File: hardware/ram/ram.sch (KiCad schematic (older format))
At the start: 16 parts, among them J1 I/O Expansion 1, J2 I/O Expansion 2, J3 DB25_Male, J4 DB37_Male, U1 71V016SA12PHGI, U2 SN74HCS00PWR, U3 SN74HCS00PWR, U4 SN74HCS00PWR, U5 SN74LVC541APWR, U6 SN74LVC541APWR

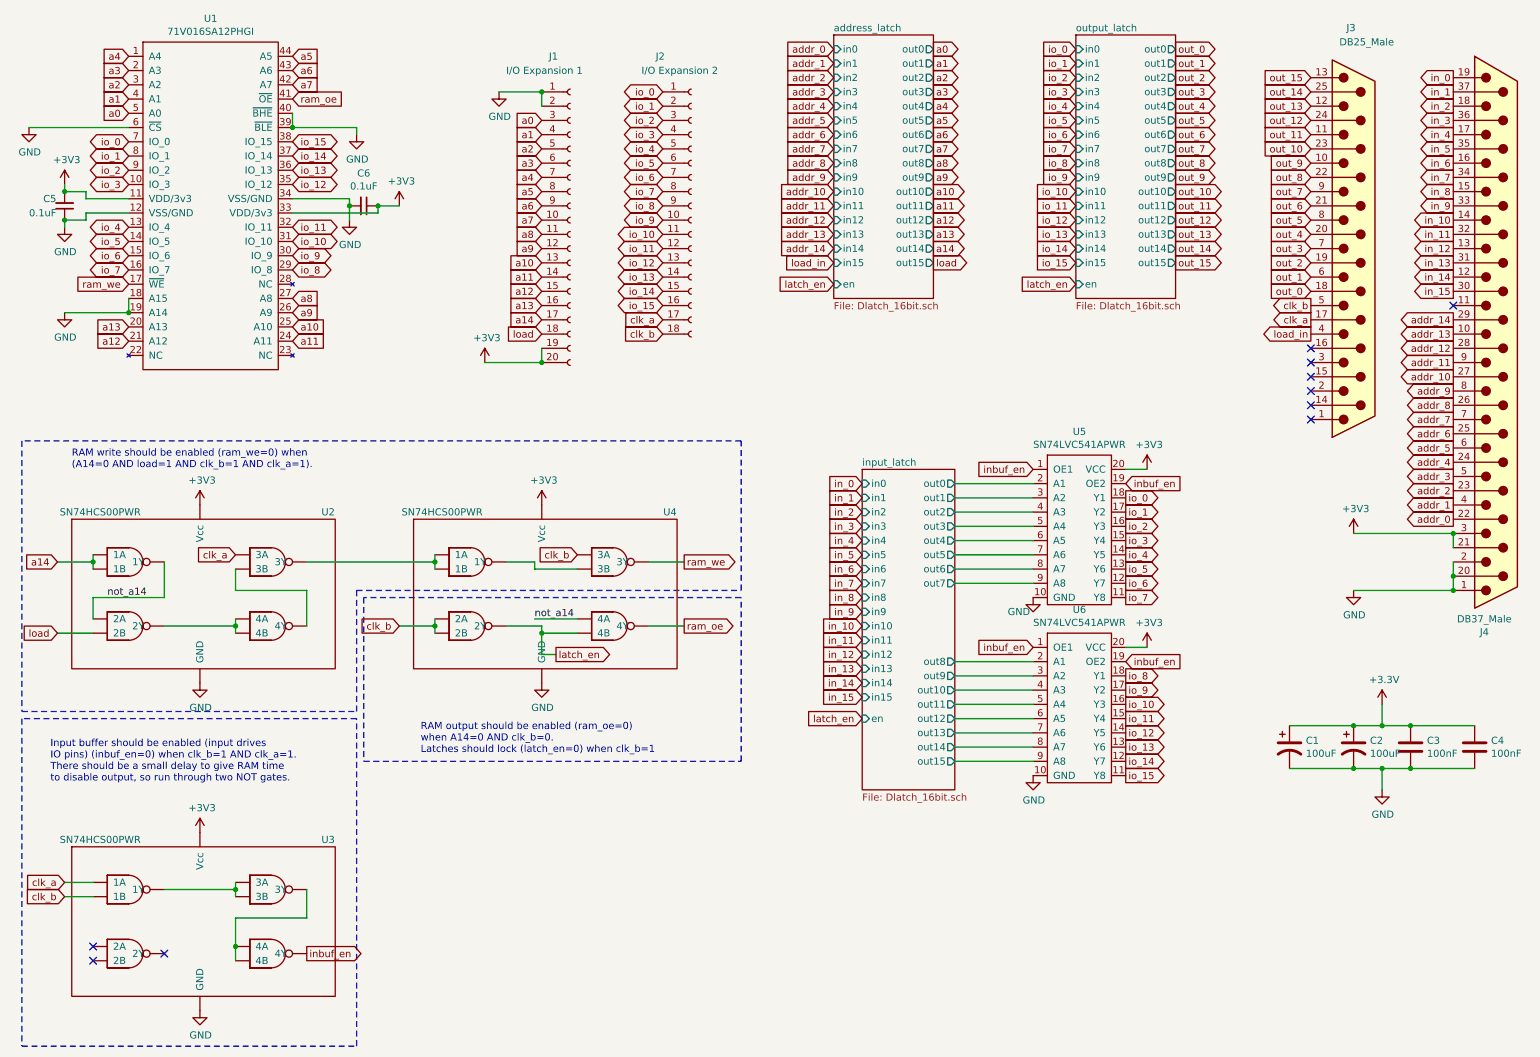
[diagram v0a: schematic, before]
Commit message: RAM board rework complete. Added COTS latch chips and Teensy 4.1 peripheral + magjack for ethernet.
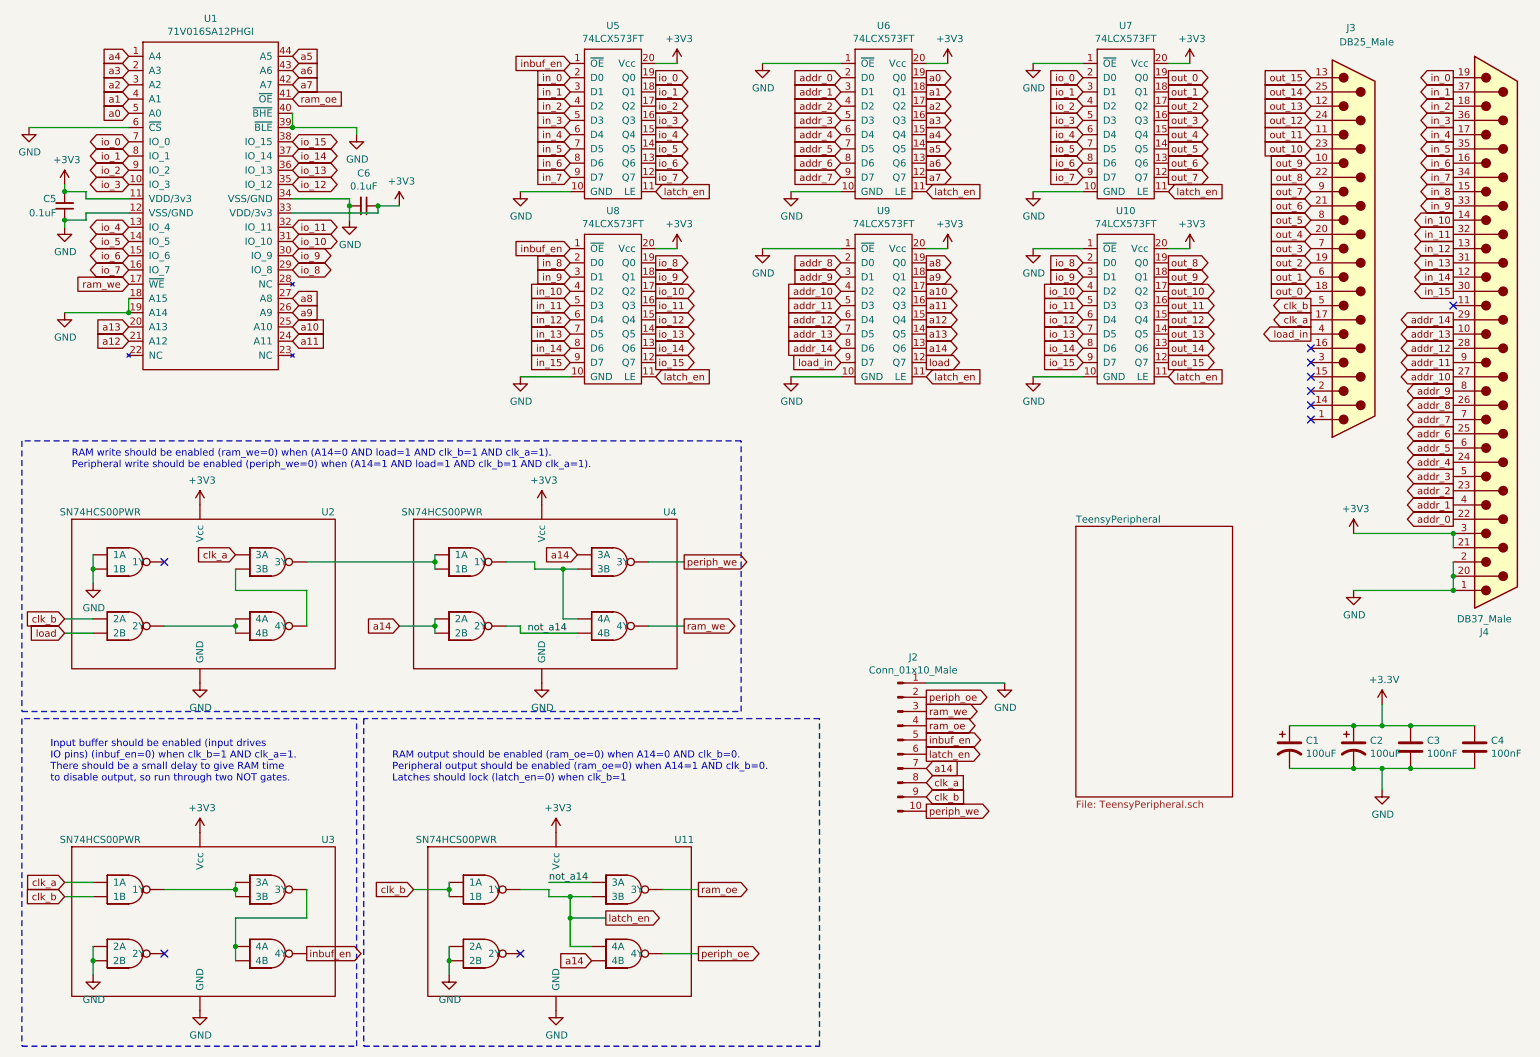
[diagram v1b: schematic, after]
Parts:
- removed J1: I/O Expansion 1, Connector_PinHeader_2.54mm:PinHeader_2x10_P2.54mm_Vertical, symbol Connector:Conn_01x20_Female
- removed J2: I/O Expansion 2, Connector_PinHeader_2.54mm:PinHeader_2x09_P2.54mm_Vertical, symbol Connector:Conn_01x18_Female
- removed U5, U6: SN74LVC541APWR, Package_SO:TSSOP-20_4.4x6.5mm_P0.65mm, symbol NANDIRL_components:SN74LVC541APWR
- added J2: Conn_01x10_Male, Connector_PinHeader_2.54mm:PinHeader_1x10_P2.54mm_Vertical, symbol Connector:Conn_01x10_Male
- added U10, U5, U6, U7, U8, U9: 74LCX573FT, Package_SO:TSSOP-20_4.4x6.5mm_P0.65mm, symbol NANDIRL_components:74LCX573FT
- added U11: SN74HCS00PWR, Package_SO:TSSOP-14_4.4x5mm_P0.65mm, symbol NANDIRL_components:SN74HCS00PWR
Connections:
- net +3V3: now also U10.20 (Vcc), U11.14 (Vcc), U5.20 (Vcc), U6.20 (Vcc), U7.20 (Vcc), U8.20 (Vcc), U9.20 (Vcc)
- net GND: now also U2.1 (1A), U2.2 (1B), U3.4 (2A), U3.5 (2B), J2.1 (Pin_1), U10.1 (~OE), U10.10 (GND), U11.4 (2A), U11.5 (2B), U11.7 (GND), U5.10 (GND), U6.1 (~OE), U6.10 (GND), U7.1 (~OE), U7.10 (GND), U8.10 (GND), U9.1 (~OE), U9.10 (GND)
- net a0: now also U6.19 (Q0)
- net a1: now also U6.18 (Q1)
- net a10: now also U9.17 (Q2)
- net a11: now also U9.16 (Q3)
- net a12: now also U9.15 (Q4)
- net a13: now also U9.14 (Q5)
- net a14: now also U4.4 (2A), U4.5 (2B), U4.9 (3A), J2.7 (Pin_7), U11.13 (4B), U9.13 (Q6); no longer U2.1 (1A), U2.2 (1B)
- net a2: now also U6.17 (Q2)
- net a3: now also U6.16 (Q3)
- net a4: now also U6.15 (Q4)
- net a5: now also U6.14 (Q5)
- net a6: now also U6.13 (Q6)
- net a7: now also U6.12 (Q7)
- net a8: now also U9.19 (Q0)
- net a9: now also U9.18 (Q1)
- net addr_0: now also U6.2 (D0)
- net addr_1: now also U6.3 (D1)
- net addr_10: now also U9.4 (D2)
- net addr_11: now also U9.5 (D3)
- net addr_12: now also U9.6 (D4)
- net addr_13: now also U9.7 (D5)
- net addr_14: now also U9.8 (D6)
- net addr_2: now also U6.4 (D2)
- net addr_3: now also U6.5 (D3)
- net addr_4: now also U6.6 (D4)
- net addr_5: now also U6.7 (D5)
- net addr_6: now also U6.8 (D6)
- net addr_7: now also U6.9 (D7)
- net addr_8: now also U9.2 (D0)
- net addr_9: now also U9.3 (D1)
- net clk_a: now also J2.8 (Pin_8)
- net clk_b: now also U2.4 (2A), J2.9 (Pin_9), U11.1 (1A), U11.2 (1B); no longer U4.4 (2A), U4.5 (2B), U4.9 (3A)
- net in_0: now also U5.2 (D0)
- net in_1: now also U5.3 (D1)
- net in_10: now also U8.4 (D2)
- net in_11: now also U8.5 (D3)
- net in_12: now also U8.6 (D4)
- net in_13: now also U8.7 (D5)
- net in_14: now also U8.8 (D6)
- net in_15: now also U8.9 (D7)
- net in_2: now also U5.4 (D2)
- net in_3: now also U5.5 (D3)
- net in_4: now also U5.6 (D4)
- net in_5: now also U5.7 (D5)
- net in_6: now also U5.8 (D6)
- net in_7: now also U5.9 (D7)
- net in_8: now also U8.2 (D0)
- net in_9: now also U8.3 (D1)
- net inbuf_en: now also J2.5 (Pin_5), U5.1 (~OE), U8.1 (~OE)
- net io_0: now also U5.19 (Q0), U7.2 (D0)
- net io_1: now also U5.18 (Q1), U7.3 (D1)
- net io_10: now also U10.4 (D2), U8.17 (Q2)
- net io_11: now also U10.5 (D3), U8.16 (Q3)
- net io_12: now also U10.6 (D4), U8.15 (Q4)
- net io_13: now also U10.7 (D5), U8.14 (Q5)
- net io_14: now also U10.8 (D6), U8.13 (Q6)
- net io_15: now also U10.9 (D7), U8.12 (Q7)
- net io_2: now also U5.17 (Q2), U7.4 (D2)
- net io_3: now also U5.16 (Q3), U7.5 (D3)
- net io_4: now also U5.15 (Q4), U7.6 (D4)
- net io_5: now also U5.14 (Q5), U7.7 (D5)
- net io_6: now also U5.13 (Q6), U7.8 (D6)
- net io_7: now also U5.12 (Q7), U7.9 (D7)
- net io_8: now also U10.2 (D0), U8.19 (Q0)
- net io_9: now also U10.3 (D1), U8.18 (Q1)
- net latch_en: now also J2.6 (Pin_6), U10.11 (LE), U11.10 (3B), U11.12 (4A), U11.3 (1Y), U5.11 (LE), U6.11 (LE), U7.11 (LE), U8.11 (LE), U9.11 (LE); no longer U4.13 (4B), U4.6 (2Y)
- net load: now also U9.12 (Q7)
- net load_in: now also U9.9 (D7)
- net not_a14: now also U4.13 (4B), U4.6 (2Y), U11.9 (3A); no longer U2.3 (1Y), U2.4 (2A), U4.12 (4A)
- net out_0: now also U7.19 (Q0)
- net out_1: now also U7.18 (Q1)
- net out_10: now also U10.17 (Q2)
- net out_11: now also U10.16 (Q3)
- net out_12: now also U10.15 (Q4)
- net out_13: now also U10.14 (Q5)
- net out_14: now also U10.13 (Q6)
- net out_15: now also U10.12 (Q7)
- net out_2: now also U7.17 (Q2)
- net out_3: now also U7.16 (Q3)
- net out_4: now also U7.15 (Q4)
- net out_5: now also U7.14 (Q5)
- net out_6: now also U7.13 (Q6)
- net out_7: now also U7.12 (Q7)
- net out_8: now also U10.19 (Q0)
- net out_9: now also U10.18 (Q1)
- net ram_oe: now also J2.4 (Pin_4), U11.8 (3Y); no longer U4.11 (4Y)
- net ram_we: now also U4.11 (4Y), J2.3 (Pin_3); no longer U4.8 (3Y)
- net at U4.10 (3B), U4.3 (1Y): now also U4.12 (4A)
- new net periph_oe: J2.2 (Pin_2), U11.11 (4Y)
- new net periph_we: J2.10 (Pin_10), U4.8 (3Y)
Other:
- note added: "RAM output should be enabled (ram_oe=0) when A14=0 AND clk_b=0.\nPeripheral output should be enabled (ram_oe=0) when A14=1 AND clk_b=0.\nLatches should lock (latch_en=0) when clk_b=1"
- note added: "RAM write should be enabled (ram_we=0) when (A14=0 AND load=1 AND clk_b=1 AND clk_a=1).\nPeripheral write should be enabled (periph_we=0) when (A14=1 AND load=1 AND clk_b=1 AND clk_a=1)."
- note removed: "RAM output should be enabled (ram_oe=0)\nwhen A14=0 AND clk_b=0.\nLatches should lock (latch_en=0) when clk_b=1"
- note removed: "RAM write should be enabled (ram_we=0) when \n(A14=0 AND load=1 AND clk_b=1 AND clk_a=1)."
